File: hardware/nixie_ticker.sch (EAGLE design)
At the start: 12 parts

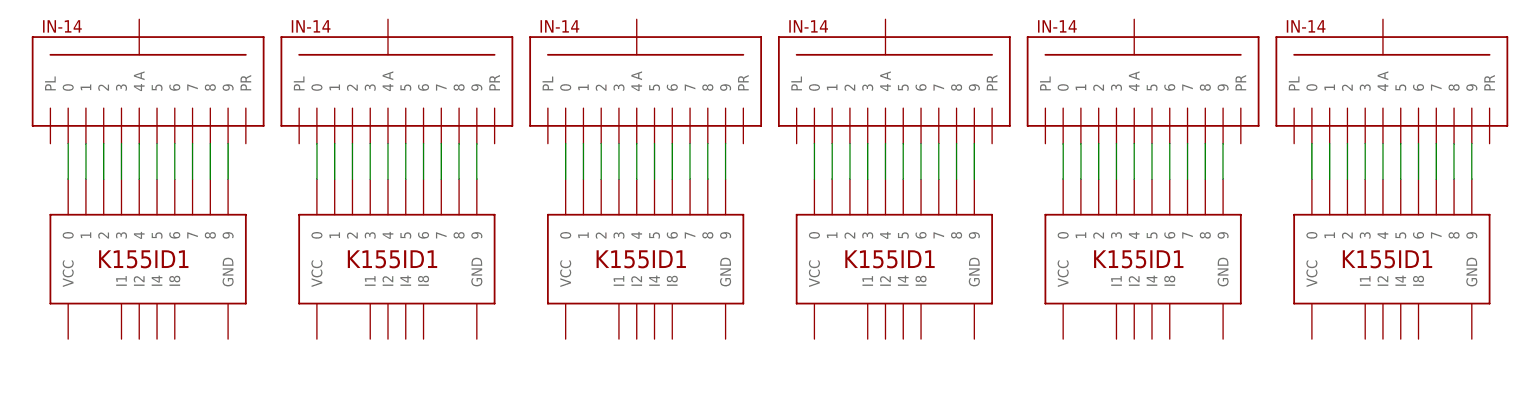
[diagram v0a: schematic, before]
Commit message: Wiring all nixie tubes using design blocks
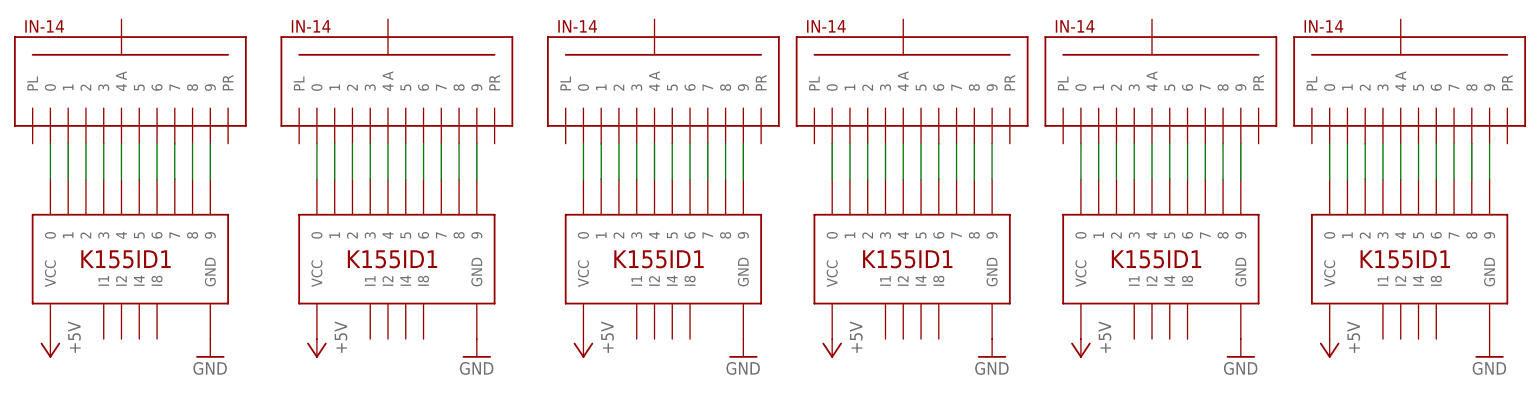
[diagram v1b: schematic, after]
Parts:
- removed U$10, U$9: K155ID1, nixie_ticker:K155ID1
- removed U$3, U$4: IN14, nixie_ticker:IN14
- added U$15, U$19: IN14, nixie_ticker:IN14
- added U$16, U$20: K155ID1, nixie_ticker:K155ID1
- U$11: value K155ID1 -> IN14; device nixie_ticker:K155ID1 -> nixie_ticker:IN14
- U$6: value IN14 -> K155ID1; device nixie_ticker:IN14 -> nixie_ticker:K155ID1
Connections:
- removed net N$21: U$3.0, U$9.0
- removed net N$22: U$3.1, U$9.1
- removed net N$23: U$3.2, U$9.2
- removed net N$24: U$3.3, U$9.3
- removed net N$25: U$3.4, U$9.4
- removed net N$26: U$3.5, U$9.5
- removed net N$27: U$3.6, U$9.6
- removed net N$28: U$3.7, U$9.7
- removed net N$29: U$3.8, U$9.8
- removed net N$30: U$3.9, U$9.9
- removed net N$41: U$11.0, U$5.0
- removed net N$42: U$11.1, U$5.1
- removed net N$43: U$11.2, U$5.2
- removed net N$44: U$11.3, U$5.3
- removed net N$45: U$11.4, U$5.4
- removed net N$46: U$11.5, U$5.5
- removed net N$47: U$11.6, U$5.6
- removed net N$48: U$11.7, U$5.7
- removed net N$49: U$11.8, U$5.8
- removed net N$50: U$11.9, U$5.9
- removed net N$51: U$12.0, U$6.0
- removed net N$52: U$12.1, U$6.1
- removed net N$53: U$12.2, U$6.2
- removed net N$54: U$12.3, U$6.3
- removed net N$55: U$12.4, U$6.4
- removed net N$56: U$12.5, U$6.5
- removed net N$57: U$12.6, U$6.6
- removed net N$58: U$12.7, U$6.7
- removed net N$59: U$12.8, U$6.8
- removed net N$60: U$12.9, U$6.9
- new net +5V: U$12.VCC, U$16.VCC, U$20.VCC, U$6.VCC, U$7.VCC, U$8.VCC
- new net GND: U$12.GND, U$16.GND, U$20.GND, U$6.GND, U$7.GND, U$8.GND
- new net N$100: U$15.9, U$16.9
- new net N$121: U$19.0, U$20.0
- new net N$122: U$19.1, U$20.1
- new net N$123: U$19.2, U$20.2
- new net N$124: U$19.3, U$20.3
- new net N$125: U$19.4, U$20.4
- new net N$126: U$19.5, U$20.5
- new net N$127: U$19.6, U$20.6
- new net N$128: U$19.7, U$20.7
- new net N$129: U$19.8, U$20.8
- new net N$130: U$19.9, U$20.9
- new net N$61: U$11.0, U$12.0
- new net N$62: U$11.1, U$12.1
- new net N$63: U$11.2, U$12.2
- new net N$64: U$11.3, U$12.3
- new net N$65: U$11.4, U$12.4
- new net N$66: U$11.5, U$12.5
- new net N$67: U$11.6, U$12.6
- new net N$68: U$11.7, U$12.7
- new net N$69: U$11.8, U$12.8
- new net N$70: U$11.9, U$12.9
- new net N$91: U$15.0, U$16.0
- new net N$92: U$15.1, U$16.1
- new net N$93: U$15.2, U$16.2
- new net N$94: U$15.3, U$16.3
- new net N$95: U$15.4, U$16.4
- new net N$96: U$15.5, U$16.5
- new net N$97: U$15.6, U$16.6
- new net N$98: U$15.7, U$16.7
- new net N$99: U$15.8, U$16.8
- net N$31: now also U$5.0, U$6.0; no longer U$10.0, U$4.0
- net N$32: now also U$5.1, U$6.1; no longer U$10.1, U$4.1
- net N$33: now also U$5.2, U$6.2; no longer U$10.2, U$4.2
- net N$34: now also U$5.3, U$6.3; no longer U$10.3, U$4.3
- net N$35: now also U$5.4, U$6.4; no longer U$10.4, U$4.4
- net N$36: now also U$5.5, U$6.5; no longer U$10.5, U$4.5
- net N$37: now also U$5.6, U$6.6; no longer U$10.6, U$4.6
- net N$38: now also U$5.7, U$6.7; no longer U$10.7, U$4.7
- net N$39: now also U$5.8, U$6.8; no longer U$10.8, U$4.8
- net N$40: now also U$5.9, U$6.9; no longer U$10.9, U$4.9

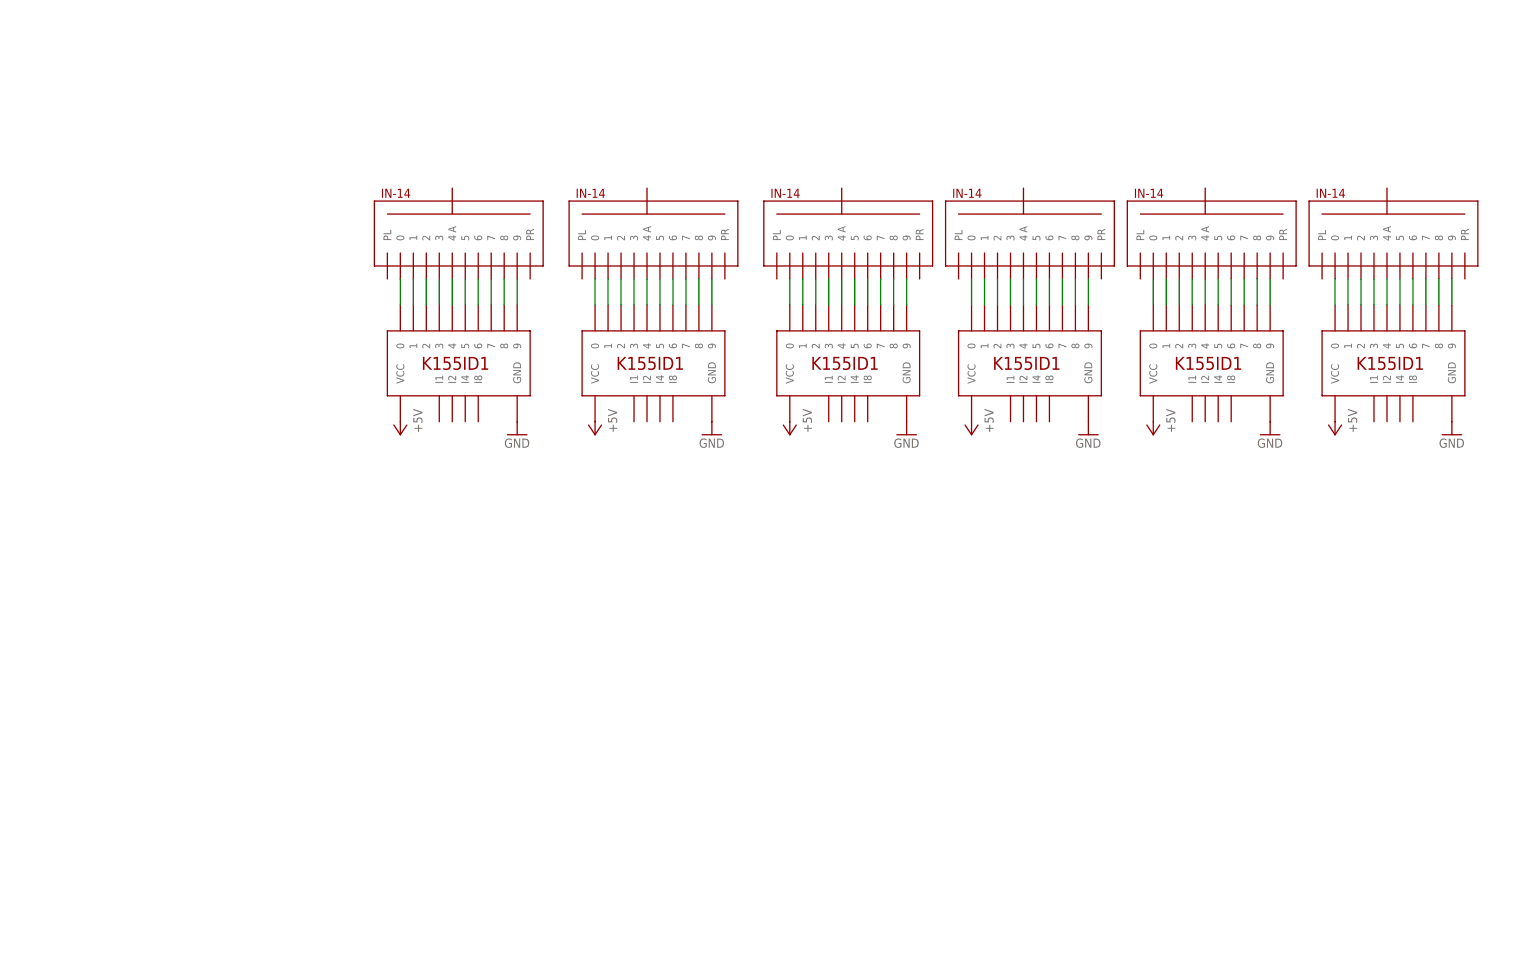
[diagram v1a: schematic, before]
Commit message: Adding high voltage logo
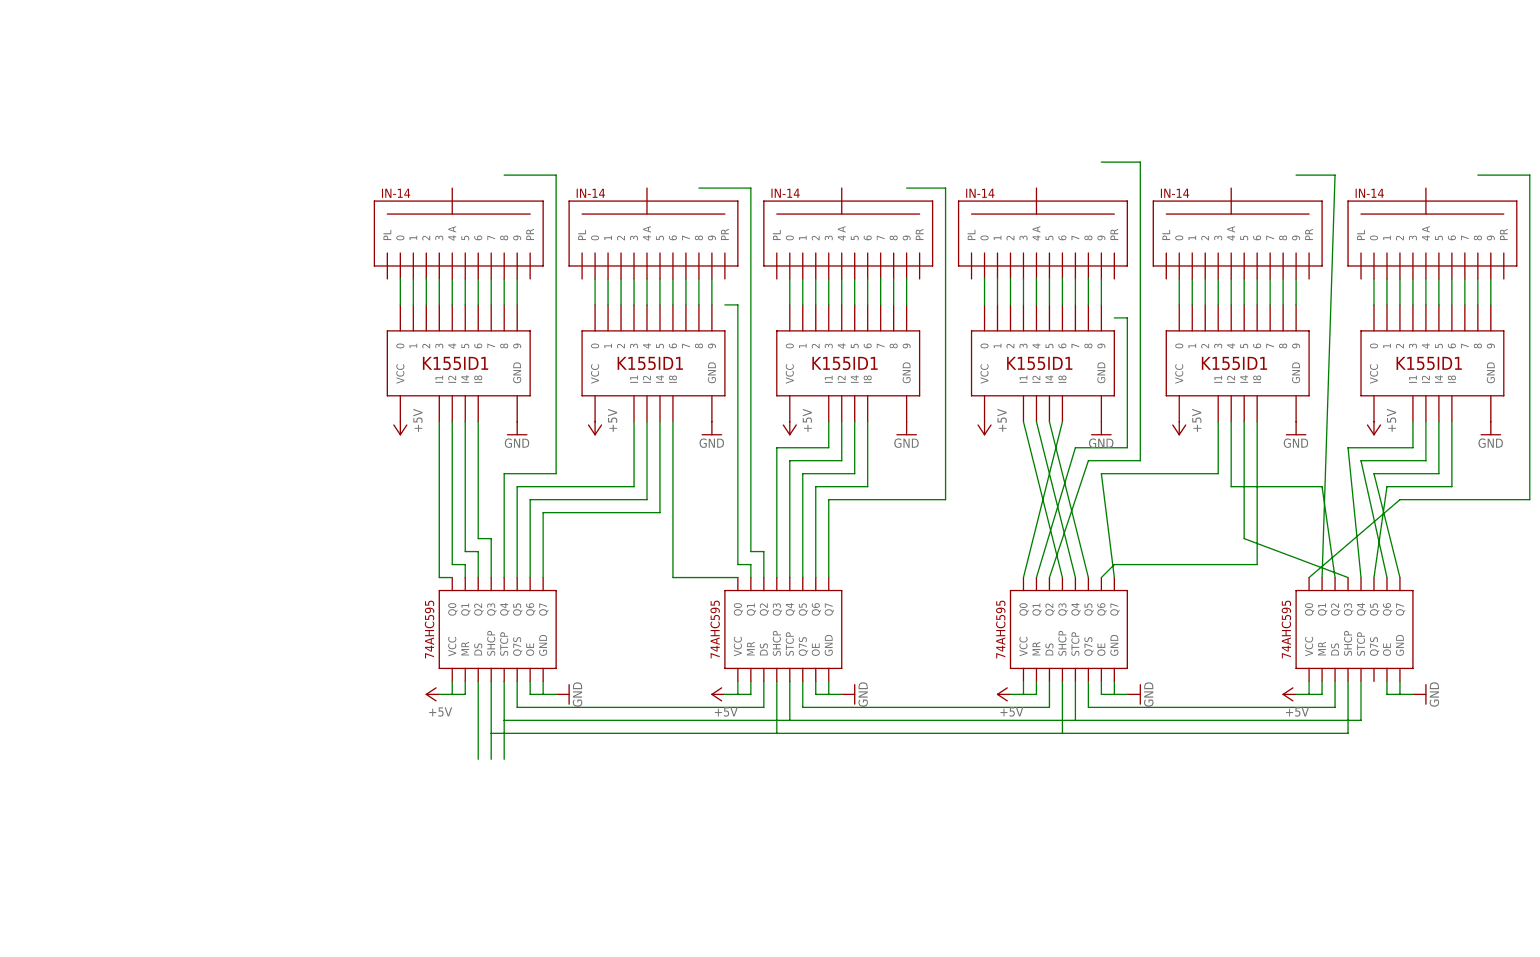
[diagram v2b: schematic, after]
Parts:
- added U$10, U$3, U$4, U$9: 74AHC595, nixie_ticker:74AHC595
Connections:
- new net N$101: U$10.Q2, U$16.I2
- new net N$21: U$4.Q7S, U$9.DS
- new net N$22: U$3.Q7S, U$4.DS
- new net N$23: U$10.DS, U$9.Q7S
- new net N$24: U$3.Q0, U$7.I1
- new net N$25: U$3.Q1, U$7.I2
- new net N$26: U$3.Q2, U$7.I4
- new net N$27: U$3.Q3, U$7.I8
- new net N$28: U$3.Q4
- new net N$29: U$3.Q5, U$8.I1
- new net N$30: U$3.Q6, U$8.I2
- new net N$41: U$3.Q7, U$8.I4
- new net N$42: U$4.Q1
- new net N$43: U$4.Q2
- new net N$44: U$4.Q3, U$6.I1
- new net N$45: U$4.Q4, U$6.I2
- new net N$46: U$4.Q5, U$6.I4
- new net N$47: U$4.Q0, U$8.I8
- new net N$48: U$4.Q6, U$6.I8
- new net N$49: U$4.Q7
- new net N$50: U$12.I1, U$9.Q3
- new net N$51: U$12.I2, U$9.Q4
- new net N$52: U$12.I4, U$9.Q5
- new net N$53: U$12.I8, U$9.Q0
- new net N$54: U$16.I1, U$9.Q7
- new net N$55: U$9.Q1
- new net N$56: U$9.Q2
- new net N$58: U$10.Q3, U$16.I4
- new net N$59: U$16.I8, U$9.Q6
- new net N$60: U$10.Q1
- new net N$81: U$10.Q4, U$20.I1
- new net N$82: U$10.Q6, U$20.I2
- new net N$83: U$10.Q7, U$20.I4
- new net N$84: U$10.Q5, U$20.I8
- new net N$85: U$10.Q0
- new net N$86: U$10.STCP, U$3.STCP, U$4.STCP, U$9.STCP
- new net N$87: U$10.SHCP, U$3.SHCP, U$4.SHCP, U$9.SHCP
- new net N$88: U$3.DS
- net +5V: now also U$10.MR, U$10.VCC, U$3.MR, U$3.VCC, U$4.MR, U$4.VCC, U$9.MR, U$9.VCC
- net GND: now also U$10.GND, U$10.OE, U$3.GND, U$3.OE, U$4.GND, U$4.OE, U$9.GND, U$9.OE

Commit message: Adding optocouplers to drive anodes
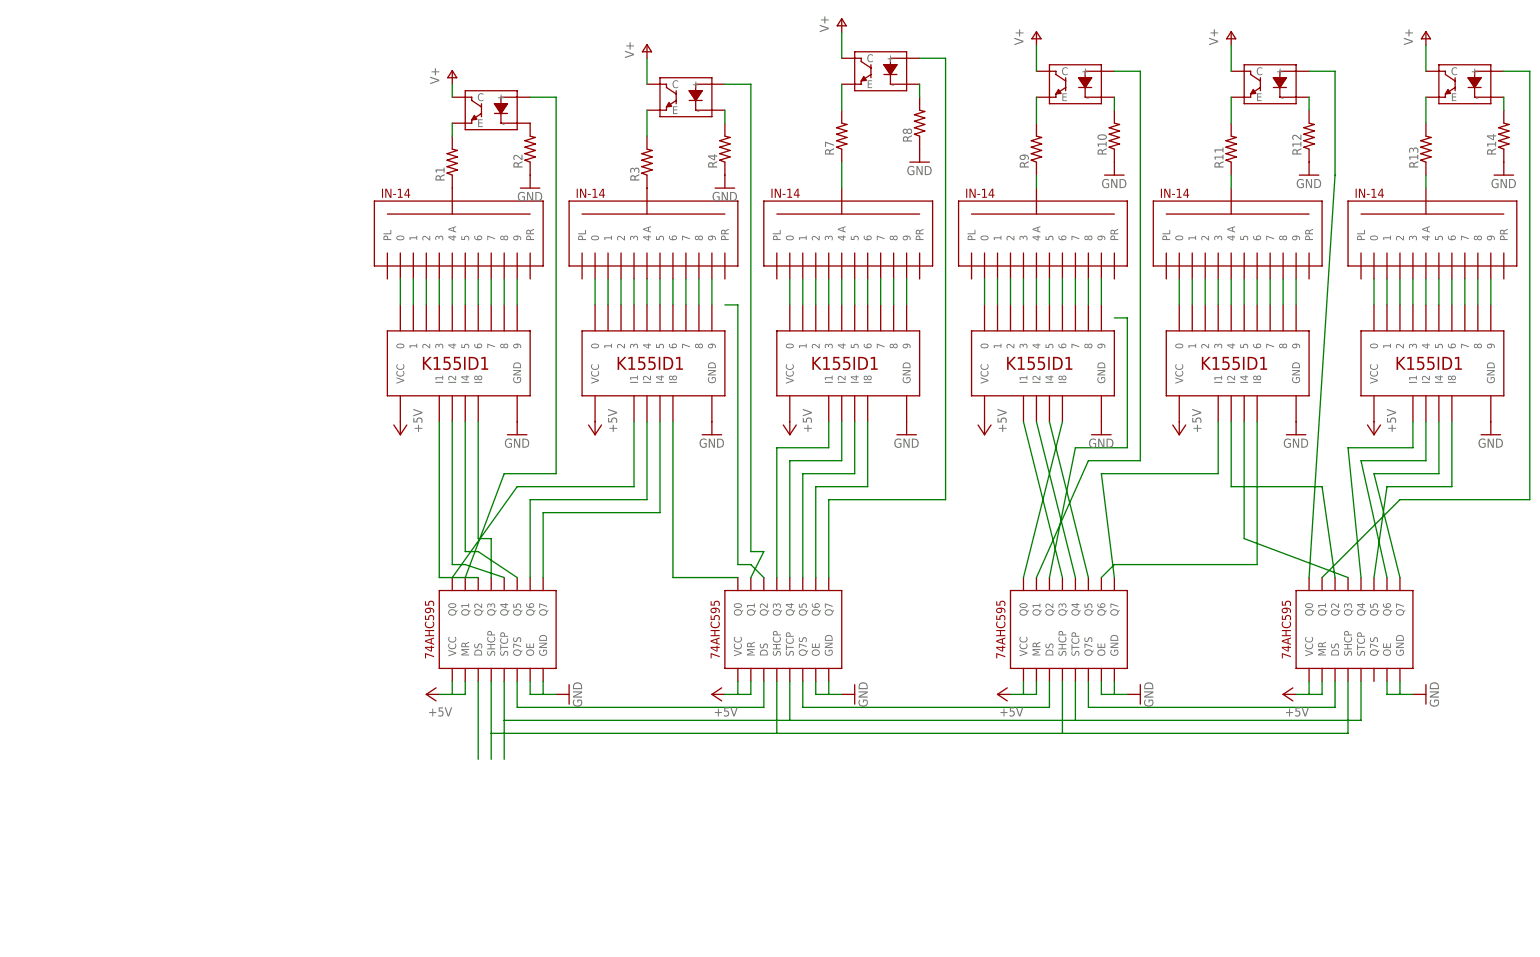
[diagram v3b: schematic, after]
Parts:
- added R1, R10, R11, R12, R13, R14, R2, R3, R4, R7, R8, R9: (no value), resistor:R-US_R0805
- added U$13, U$14, U$18, U$21, U$22, U$23: TLP387, nixie_ticker:TLP387
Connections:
- removed net N$42 (its old number): U$4.Q1
- removed net N$55 (its old number): U$9.Q1
- new net N$102: R1.2, U$13.E
- new net N$103: R2.2, U$13.-
- new net N$104: R13.1, U$19.A
- new net N$105: R3.1, U$2.A
- new net N$106: R3.2, U$14.E
- new net N$107: R4.2, U$14.-
- new net N$112: R7.2, U$18.E
- new net N$113: R8.2, U$18.-
- new net N$118: R7.1, U$5.A
- new net N$119: R9.2, U$21.E
- new net N$120: R10.2, U$21.-
- new net N$145: R9.1, U$11.A
- new net N$146: R11.2, U$22.E
- new net N$147: R12.2, U$22.-
- new net N$153: R13.2, U$23.E
- new net N$154: R14.2, U$23.-
- new net N$43: U$14.+, U$4.Q1
- new net N$56: U$21.+, U$9.Q1
- new net N$57: R1.1, U$1.A
- new net N$90: R11.1, U$15.A
- new net V+: U$13.C, U$14.C, U$18.C, U$21.C, U$22.C, U$23.C
- net GND: now also R10.1, R12.1, R14.1, R2.1, R4.1, R8.1
- net N$24: now also U$3.Q2; no longer U$3.Q0
- net N$25: now also U$3.Q4; no longer U$3.Q1
- net N$26: now also U$3.Q5; no longer U$3.Q2
- net N$28: now also U$13.+, U$3.Q1; no longer U$3.Q4
- net N$29: now also U$3.Q0; no longer U$3.Q5
- net N$49: now also U$18.+
- net N$60: now also U$10.Q0, U$22.+; no longer U$10.Q1
- net N$85: now also U$10.Q1, U$23.+; no longer U$10.Q0

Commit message: Updates 6-29
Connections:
- net N$42: now also U$4.Q5; no longer U$4.Q2
- net N$43: now also U$4.Q2; no longer U$4.Q1
- net N$45: now also U$4.Q6; no longer U$4.Q4
- net N$46: now also U$4.Q7; no longer U$4.Q5
- net N$48: now also U$4.Q4; no longer U$4.Q6
- net N$49: now also U$4.Q1; no longer U$4.Q7

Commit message: Updates 6-29
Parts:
- added C1, C10, C11, C12, C13, C14, C2, C3, C4, C5, C6, C7, C8, C9: (no value), resistor:C-USC0402
- added R15, R16, R5, R6: (no value), resistor:R-US_R0402
- added SV1: (no value), con-lstb:MA03-2
- added U$17, U$24: ZKFDS, nixie_ticker:ZKFDS
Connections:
- new net N$108: C2.1, R6.1, U$4.MR
- new net N$109: C1.1, R5.1, U$3.MR
- new net N$110: C3.1, R15.1, U$9.MR
- new net N$111: C8.1, R16.1, U$10.MR
- new net N$159: SV1.4
- net +5V: now also C10.1, C11.1, C12.1, C13.1, C14.1, C4.1, C5.1, C6.1, C7.1, C9.1, R15.2, R16.2, R5.2, R6.2, SV1.6; no longer U$10.MR, U$3.MR, U$4.MR, U$9.MR
- net GND: now also C1.2, C10.2, C11.2, C12.2, C13.2, C14.2, C2.2, C3.2, C4.2, C5.2, C6.2, C7.2, C8.2, C9.2, SV1.2, U$24.P$1
- net N$86: now also SV1.1
- net N$87: now also SV1.3
- net N$88: now also SV1.5
- net V+: now also U$17.P$1

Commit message: Finalizing board 7-1
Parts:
- removed SV1: (no value), con-lstb:MA03-2
- added C15, C16: (no value), resistor:C-USC0402
- added JP1: (no value), pinhead:PINHD-1X6
- added Q1, Q2: BCX19SMD, transistor-npn:BCX19SMD
- added R17, R18: (no value), resistor:R-US_R0805
- added U$25: CD40109B, nixie_ticker:CD40109B
- U$13, U$14, U$18, U$21, U$22, U$23: value TLP387 -> TLP3873D; device nixie_ticker:TLP387 -> nixie_ticker:TLP3873D
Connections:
- new net +3V3: C16.1, JP1.3, U$25.EN, U$25.VCC
- new net N$152: JP1.4, U$25.A
- new net N$160: Q1.C, R18.1
- new net N$161: Q2.C, R17.1
- new net N$162: R17.2, U$11.PR
- new net N$163: R18.2, U$2.PR
- net +5V: now also C15.1, JP1.2, U$25.VDD; no longer SV1.6
- net GND: now also C15.2, C16.2, JP1.1, Q1.E, Q2.E, U$25.VSS; no longer SV1.2
- net N$159: now also JP1.6, U$25.C; no longer SV1.4
- net N$22: now also U$25.G
- net N$42: now also Q1.B, U$4.Q3; no longer U$4.Q5
- net N$44: now also U$4.Q4; no longer U$4.Q3
- net N$48: now also U$4.Q5; no longer U$4.Q4
- net N$55: now also Q2.B
- net N$86: now also U$25.E; no longer SV1.1
- net N$87: now also U$25.F; no longer SV1.3
- net N$88: now also JP1.5, U$25.B; no longer SV1.5, U$3.DS
